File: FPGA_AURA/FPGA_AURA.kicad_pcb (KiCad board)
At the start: 10 copper layers, 50 x 50 mm, 172 parts, among them J700 SS5-40-3.50-X-D-K-XX, J701 SS5-20-3.50-X-D-K-XX, U1 XC7A35T-2FTG256C, U100 ADP5014, U2 W25Q256JVEIQ, U4 TPS51200DRCR, U500 MT41K128M16JT-125_IT_K, Y500 ASEM1-100.000MHZ-LC-T

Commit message: All components placed, routing left to do followed by final checks.
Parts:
- C414, C416, C419, C423, C425, C426, C427, C428, C430: footprint Capacitor_SMD:C_0402_1005Metric -> Capacitor_SMD:C_0201_0603Metric; moved to B.Cu
- R422: value 81R -> 91R; footprint Resistor_SMD:R_0402_1005Metric -> Resistor_SMD:R_0201_0603Metric
- R423: moved to F.Cu
- R425: moved to B.Cu
- moved R300 73.7 mm to (145.8, 90.6)
- moved C427 36.8 mm to (111.3, 68.7), turned to -90 degrees
- moved C428 35.5 mm to (119.8, 68.6), turned to 0 degrees
- moved C430 35.3 mm to (114.1, 68.2), turned to 0 degrees
- moved C425 34.9 mm to (118.2, 68.6), turned to 180 degrees
- moved C423 30.9 mm to (110.2, 69.1), turned to 0 degrees
- moved R425 30.7 mm to (115.5, 59.5)
- moved C426 29.2 mm to (113.8, 62.3), turned to -90 degrees
- moved R422 23.2 mm to (113.8, 67.3)
- moved C419 23.1 mm to (109.9, 60.9), turned to 0 degrees
- moved C414 22.4 mm to (117.8, 60.9), turned to 0 degrees
- moved R424 16.1 mm to (108.0, 59.1), turned to 90 degrees
- moved R423 11.6 mm to (107.0, 59.1), turned to 90 degrees
- moved C416 4.00 mm to (111.3, 60.9), turned to 180 degrees
- moved C412 0.20 mm to (122.9, 67.8), turned to 90 degrees
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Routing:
- net GND: track 93.2 -> 119.2 mm, vias 174 -> 178
- net +1V35: track 19.0 -> 38.9 mm
- net +1V8: track 11.2 -> 15.0 mm, vias 15 -> 17
- net SDA_1V8: track 15.0 -> 18.8 mm, vias 1 -> 2
- net DDR3_A12: track 71.7 -> 75.3 mm
- net UART_1V8_0_TX: track 12.8 -> 16.1 mm, vias 1 -> 2
- net DDR3_BA1: track 84.4 -> 87.7 mm
- net DDR3_A1: track 71.9 -> 74.9 mm
- net SCL_1V8: track 13.6 -> 16.6 mm, vias 1 -> 2
- net DDR3_A2: track 72.4 -> 75.4 mm
- net UART_1V8_1_TX: track 10.8 -> 13.5 mm
- net +3V3: track 15.9 -> 18.5 mm, vias 23 -> 24
- net UART_1V8_0_RX: track 11.1 -> 13.7 mm, vias 1 -> 2
- net DDR3_A6: track 84.4 -> 87.0 mm
- net DDR3_A10: track 72.3 -> 74.8 mm
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
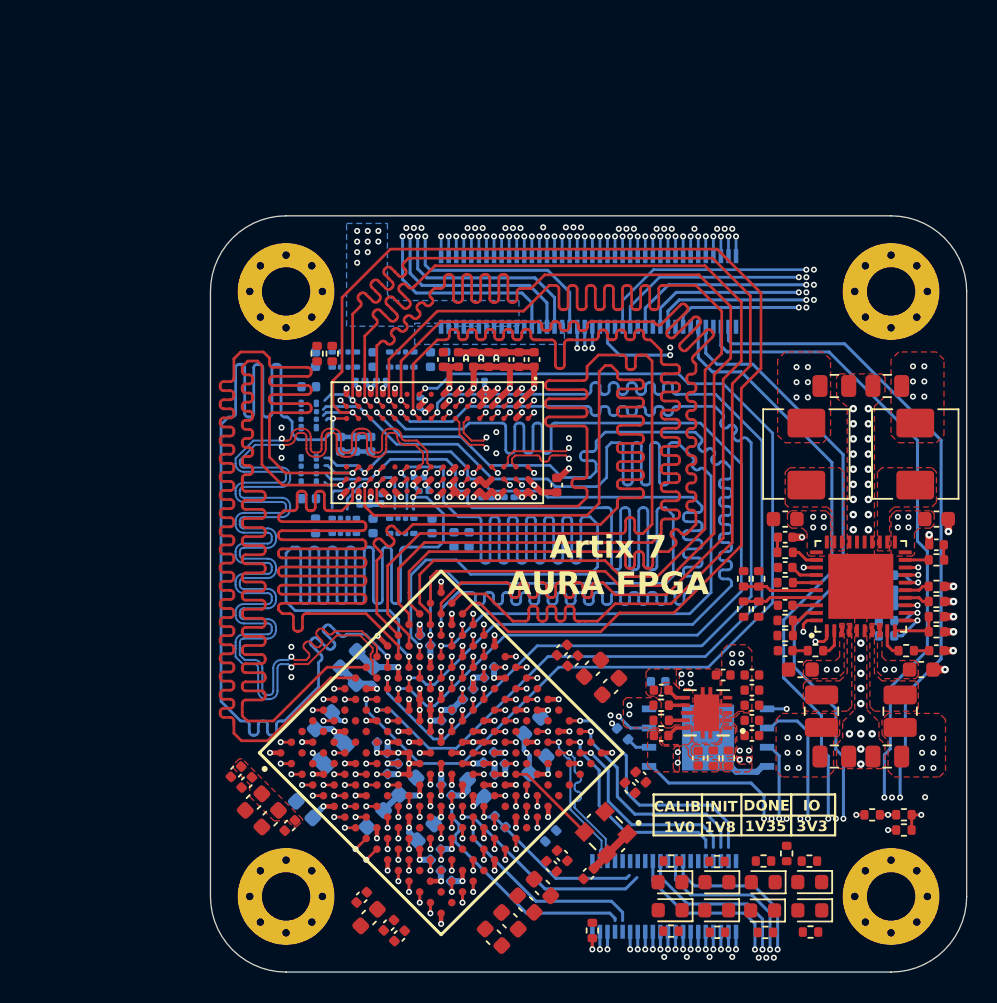
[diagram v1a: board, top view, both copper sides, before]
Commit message: Power planes done on layers 3 and 4 as well as almost all mezzanine connections made. QSPI and misc left to do.
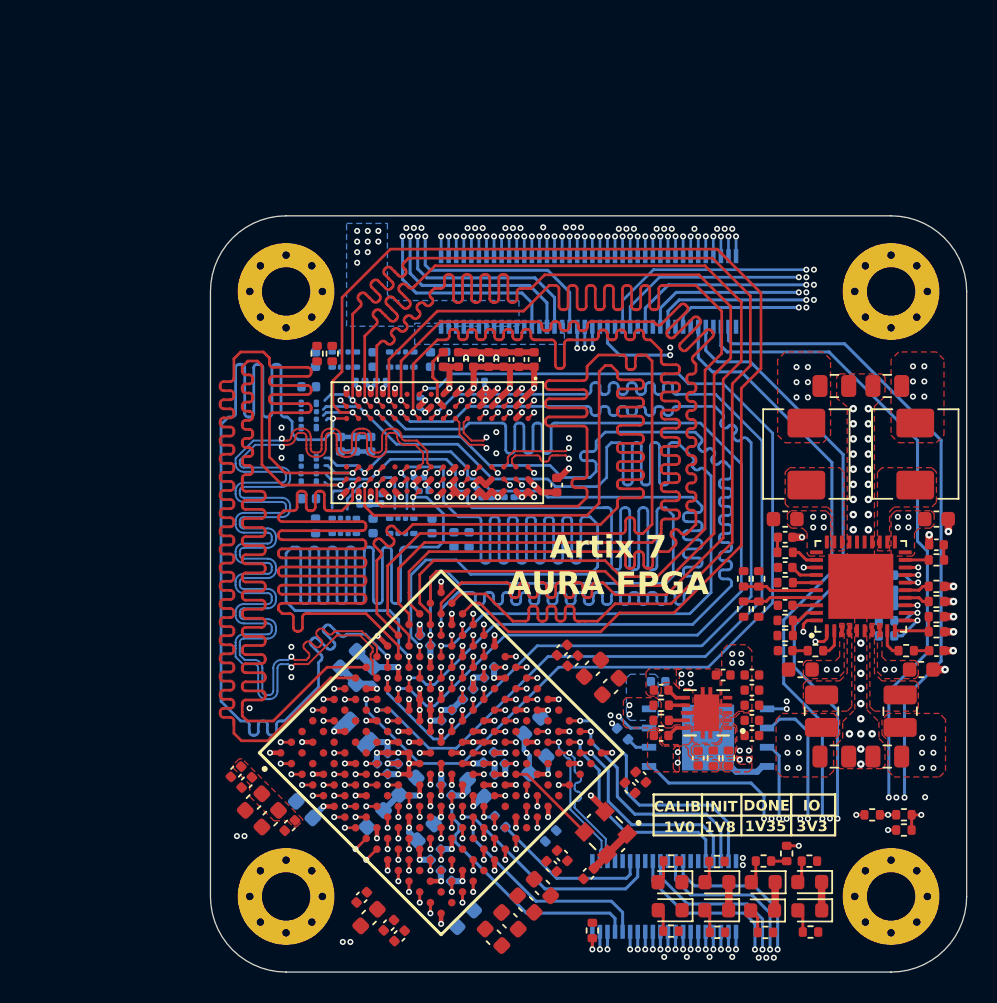
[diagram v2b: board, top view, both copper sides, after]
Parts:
- moved C211 16.1 mm to (116.8, 96.5), turned to 45 degrees
- moved C201 2.09 mm to (109.8, 84.2), turned to 135 degrees
- moved C204 0.69 mm to (111.3, 85.8), turned to -135 degrees
- turned R303 to 135 degrees
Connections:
- J701 pad 08: TMS -> TCK
- J701 pad 10: TCK -> TDI
- J701 pad 11: TDI -> TDO
- J701 pad 13: TDO -> TMS
- J701 pad 31: SPI_SD_CS_0 -> SPI_SD_SCK
- J701 pad 33: SPI_SD_SCK -> SPI_SD_MISO
- J701 pad 37: SPI_SD_MISO -> SPI_SD_CS_0
- R303 pad 2: TDO -> /300_FPGA_Config/TDO_R
- U1 pad M1: SPI_1V8_CS_1 -> SPI_1V8_SCK
- U1 pad M2: SPI_1V8_CS_2 -> SPI_1V8_MOSI
- U1 pad M4: SPI_1V8_CS_3 -> UART_1V8_0_RX
- U1 pad M5: SDA_1V8 -> UART_1V8_1_TX
- U1 pad M6: SPI_3V3_SCK -> SPI_3V3_MISO
- U1 pad N1: SPI_1V8_SCK -> UART_1V8_0_TX
- U1 pad N3: SPI_1V8_CS_0 -> SPI_1V8_MISO
- U1 pad N4: SCL_1V8 -> UART_1V8_1_RX
- U1 pad N6: SPI_3V3_MOSI -> CAN_TX
- U1 pad N8: TDO -> /300_FPGA_Config/TDO_R
- U1 pad N9: SPI_3V3_CS_0 -> SPI_3V3_CS_2
- U1 pad P1: SPI_1V8_MOSI -> SDA_1V8
- U1 pad P10: CAN_TX -> unconnected-(U1C-IO_L14P_T2_SRCC_14-PadP10)
- U1 pad P11: CAN_RX -> SPI_3V3_SCK
- U1 pad P4: SPI_1V8_MISO -> SPI_1V8_CS_0
- U1 pad P8: SPI_3V3_MISO -> UART_3V3_1_RX
- U1 pad R1: UART_1V8_0_TX -> SPI_1V8_CS_2
- U1 pad R10: SPI_3V3_CS_2 -> SCL_3V3
- U1 pad R11: SPI_3V3_CS_1 -> SPI_3V3_CS_0
- U1 pad R3: UART_1V8_0_RX -> SCL_1V8
- U1 pad R5: UART_3V3_0_RX -> CAN_RX
- U1 pad R6: UART_3V3_1_TX -> UART_3V3_0_TX
- U1 pad R7: UART_3V3_1_RX -> UART_3V3_0_RX
- U1 pad T10: UART_3V3_0_TX -> SPI_3V3_CS_1
- U1 pad T13: unconnected-(U1C-IO_L16N_T2_A15_D31_14-PadT13) -> SPI_3V3_MOSI
- U1 pad T3: UART_1V8_1_RX -> SPI_1V8_CS_1
- U1 pad T4: UART_1V8_1_TX -> SPI_1V8_CS_3
- U1 pad T7: SDA_3V3 -> UART_3V3_1_TX
- U1 pad T8: SCL_3V3 -> SDA_3V3
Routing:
- net SCL_1V8: track 16.6 -> 93.0 mm
- net SDA_1V8: track 18.8 -> 94.3 mm
- net UART_1V8_0_TX: track 16.1 -> 87.9 mm
- net SPI_1V8_CS_3: track 14.3 -> 81.6 mm, vias 2 -> 4
- net SPI_1V8_CS_1: track 14.6 -> 75.1 mm
- net SPI_1V8_CS_2: track 14.6 -> 73.8 mm
- net SPI_1V8_CS_0: track 15.2 -> 73.6 mm, vias 2 -> 3
- net UART_1V8_0_RX: track 13.7 -> 72.0 mm
- net UART_1V8_1_RX: track 10.6 -> 68.3 mm
- net UART_1V8_1_TX: track 13.5 -> 70.6 mm
- net SPI_1V8_MISO: track 6.26 -> 59.8 mm
- net SPI_1V8_SCK: track 2.07 -> 55.0 mm
- net SPI_1V8_MOSI: track 2.07 -> 54.2 mm
- net +VREF: track 7.93 -> 39.5 mm
- net SPI_3V3_SCK: track 11.5 -> 33.1 mm
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- added copper zone on In3.Cu, net +1V0
- added copper zone on In2.Cu, net +1V35
- added copper zone on In3.Cu, net +1V8
- added copper zone on B.Cu, net +3V3
- added copper zone on In2.Cu, net +3V3
- added copper zone on In2.Cu, net +5V
- added copper zone on In2.Cu, net +VTT

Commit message: Continued routing, getting close to finishing. 1 Error found: DDR VREF shares same net as VREF of buck.
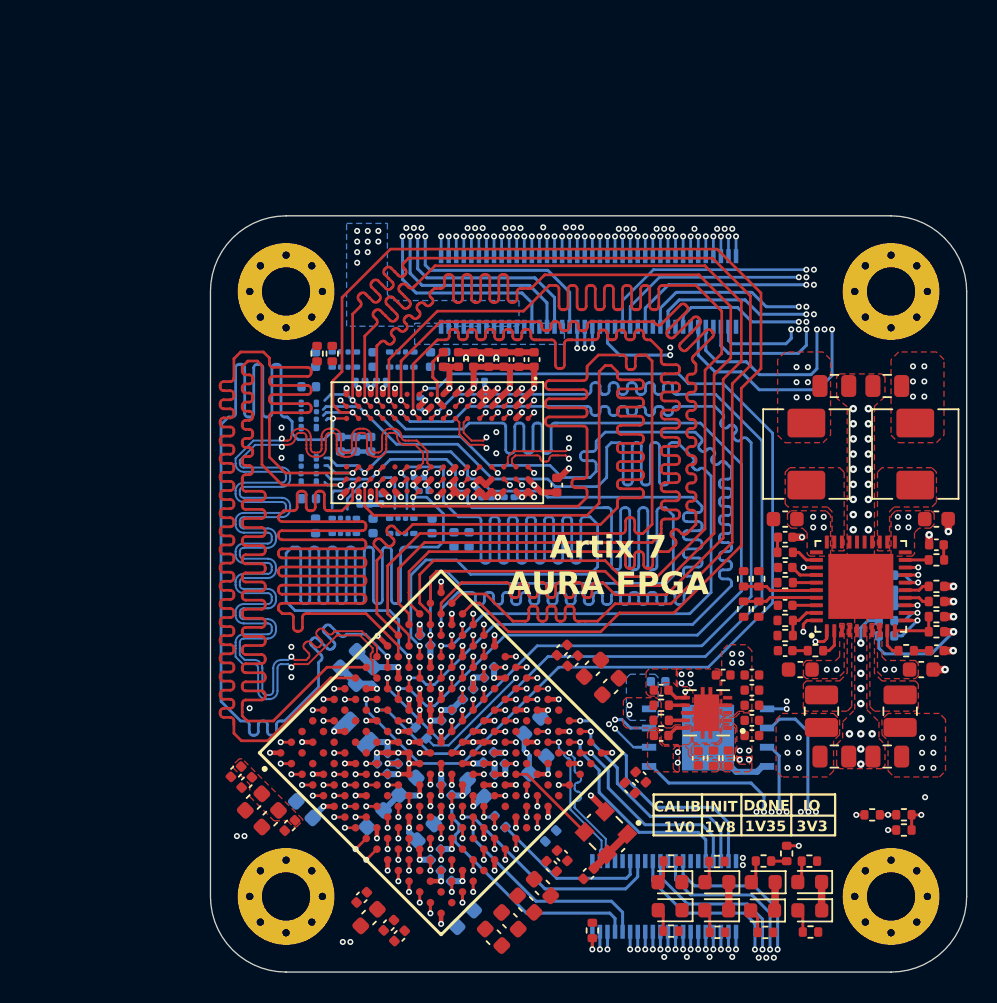
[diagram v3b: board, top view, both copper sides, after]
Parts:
- moved R304 13.3 mm to (113.9, 84.2)
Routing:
- net +VREF: track 39.5 -> 82.0 mm, vias 3 -> 4
- net /300_FPGA_Config/QSPI_IO1: track 9.75 -> 32.9 mm
- net /300_FPGA_Config/QSPI_CLK: track 1.61 -> 23.4 mm, vias 0 -> 2
- net /300_FPGA_Config/QSPI_IO0: track 10.6 -> 30.5 mm
- net /300_FPGA_Config/QSPI_IO2: track 6.16 -> 25.7 mm
- net PHY_0_RST: track 40.4 -> 56.7 mm
- net PHY_1_RST: track 40.8 -> 53.8 mm
- net MDC: track 42.5 -> 51.8 mm
- net /300_FPGA_Config/QSPI_IO3: track 2.32 -> 9.51 mm, vias 1 -> 2
- net +3V3: track 19.3 -> 25.8 mm
- net GND: track 126.1 -> 131.9 mm, vias 184 -> 185
- net MDIO: track 43.0 -> 48.2 mm
- net SPI_SD_SCK: track 14.8 -> 14.3 mm
- net SPI_SD_MISO: track 13.9 -> 13.4 mm
- net SPI_SD_MOSI: track 15.6 -> 15.1 mm
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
